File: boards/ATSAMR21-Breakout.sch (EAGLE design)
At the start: 20 parts, among them IC1 MCP73831T-2ATI/OT, IC2 LTC4412, IC3 NCP4589DSN33T1G, IC4 ATSAMR21G18-MR210UA, Q1 SI2301CDS-T1-GE3

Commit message: Added breakout board for ATZB-RF-233-1-C.
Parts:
- C1: value TPSB107M010R0400 -> 10uF
- C2: value TPSB107M010R0400 -> 47uF
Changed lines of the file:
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@@
 <?xml version="1.0" encoding="utf-8"?>
 <!DOCTYPE eagle SYSTEM "eagle.dtd">
-<eagle version="7.4.0">
+<eagle version="7.7.0">
 <drawing>
 <settings>
@@
 <part name="D1" library="custom_components" deviceset="1N5819HW-7-F" device=""/>
 <part name="Q1" library="SparkFun-DiscreteSemi" deviceset="MOSFET-PCHANNEL" device="" value=" SI2301CDS-T1-GE3 "/>
-<part name="C1" library="custom_componentsv0.9" deviceset="TPSB107M010R0400" device=""/>
+<part name="C1" library="custom_componentsv0.9" deviceset="TPSB107M010R0400" device="" value="10uF"/>
 <part name="GND5" library="SparkFun-Aesthetics" deviceset="GND" device=""/>
 <part name="GND6" library="SparkFun-Aesthetics" deviceset="GND" device=""/>
-<part name="C2" library="custom_componentsv0.9" deviceset="TPSB107M010R0400" device=""/>
+<part name="C2" library="custom_componentsv0.9" deviceset="TPSB107M010R0400" device="" value="47uF"/>
 <part name="IC1" library="custom_components" deviceset="MCP73831T-2ATI/OT" device=""/>
 <part name="GND7" library="SparkFun-Aesthetics" deviceset="GND" device=""/>

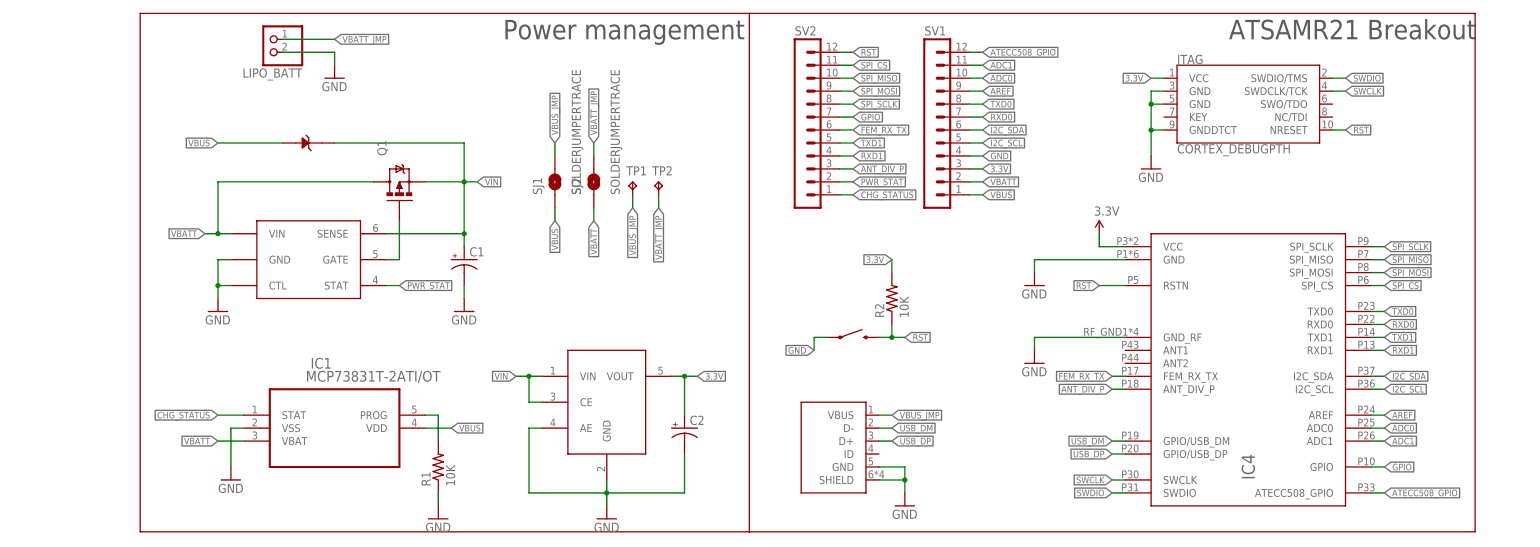
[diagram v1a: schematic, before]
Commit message: Changed Power-Path design.
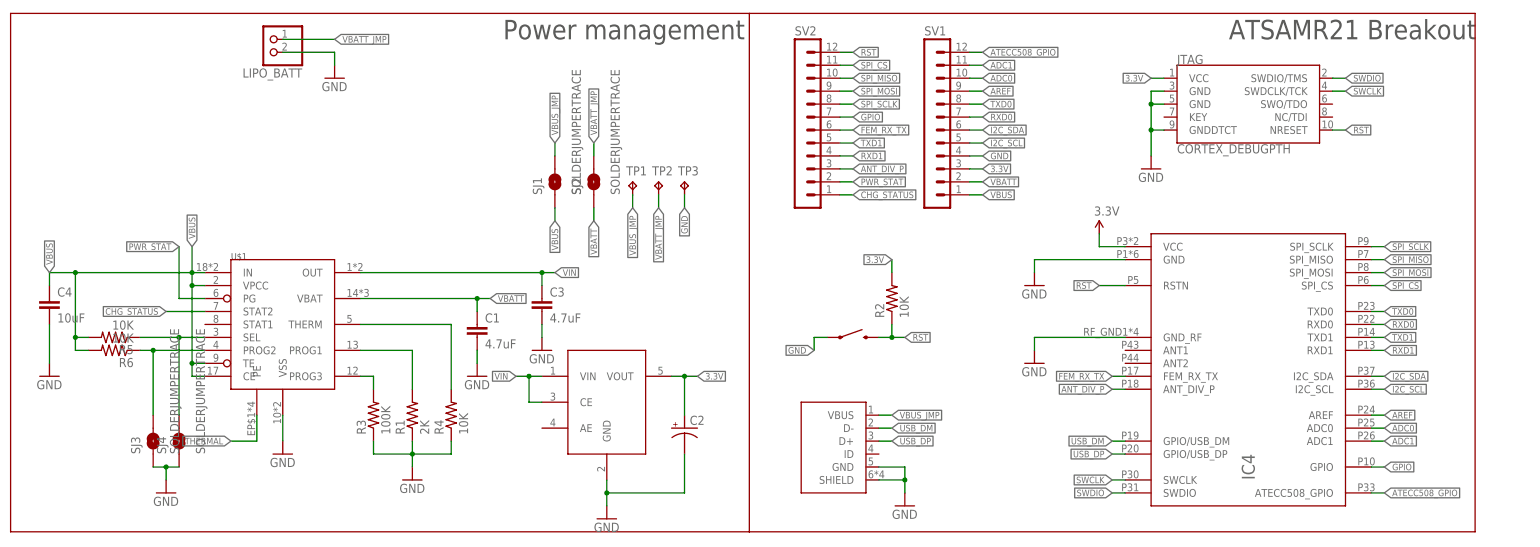
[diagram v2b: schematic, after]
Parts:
- removed D1: 1N5819HW-7-F, custom_components:1N5819HW-7-F
- removed IC1: MCP73831T-2ATI/OT, custom_components:MCP73831T-2ATI/OT
- removed IC2: LTC4412, custom_components:LTC4412
- removed Q1: SI2301CDS-T1-GE3, SparkFun-DiscreteSemi:MOSFET-PCHANNEL
- added C3: 4.7uF, SparkFun-Capacitors:22UF-0805-6.3V-20%
- added C4: 10uF, SparkFun-Capacitors:22UF-0805-6.3V-20%
- added R3: 100K, SparkFun-Resistors:RESISTOR0805-RES
- added R4, R5, R6: 10K, SparkFun-Resistors:RESISTOR0805-RES
- added SJ3, SJ4: SOLDERJUMPERTRACE, SparkFun-Retired:SOLDERJUMPERTRACE
- added TP3: TPB2,54, testpad:TPB2,54
- added U$1: MCP73871T, radios:MCP73871T
- C1: value 10uF -> 4.7uF; device custom_componentsv0.9:TPSB107M010R0400 -> SparkFun-Capacitors:22UF-0805-6.3V-20%
- R1: value 10K -> 2K
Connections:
- removed net N$8: IC1.PROG, R1.2
- new net N$2: R5.1, SJ4.2, U$1.SEL
- new net N$3: R3.2, U$1.PROG3
- new net N$4: R1.2, U$1.PROG1
- new net N$5: R4.2, U$1.THERM
- new net THERMAL: U$1.PE
- net CHG_STATUS: now also U$1.STAT2; no longer IC1.STAT
- net GND: now also C1.2, C3.2, C4.2, R3.1, R4.1, SJ3.1, SJ4.1, TP3.TP, U$1.VSS; no longer C1.-, IC1.VSS, IC2.CTL, IC2.GND, IC3.AE
- net N$1: now also R6.1, SJ3.2, U$1.PROG2; no longer IC2.GATE, Q1.G
- net PWR_STAT: now also U$1.PG; no longer IC2.STAT
- net VBATT: now also C1.1, U$1.VBAT; no longer IC1.VBAT, IC2.VIN, Q1.D
- net VBUS: now also C4.1, R5.2, R6.2, U$1.CE, U$1.IN, U$1.TE, U$1.VPCC; no longer D1.ANODE, IC1.VDD
- net VIN: now also C3.1, U$1.OUT; no longer C1.+, D1.CATHODE, IC2.SENSE, Q1.S
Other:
- moved on the sheet: R1
